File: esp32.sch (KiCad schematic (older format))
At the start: 5 parts, among them IC1 ESP32-WROVER-E_M213EH6464PH3Q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, J4 Bus_Connector

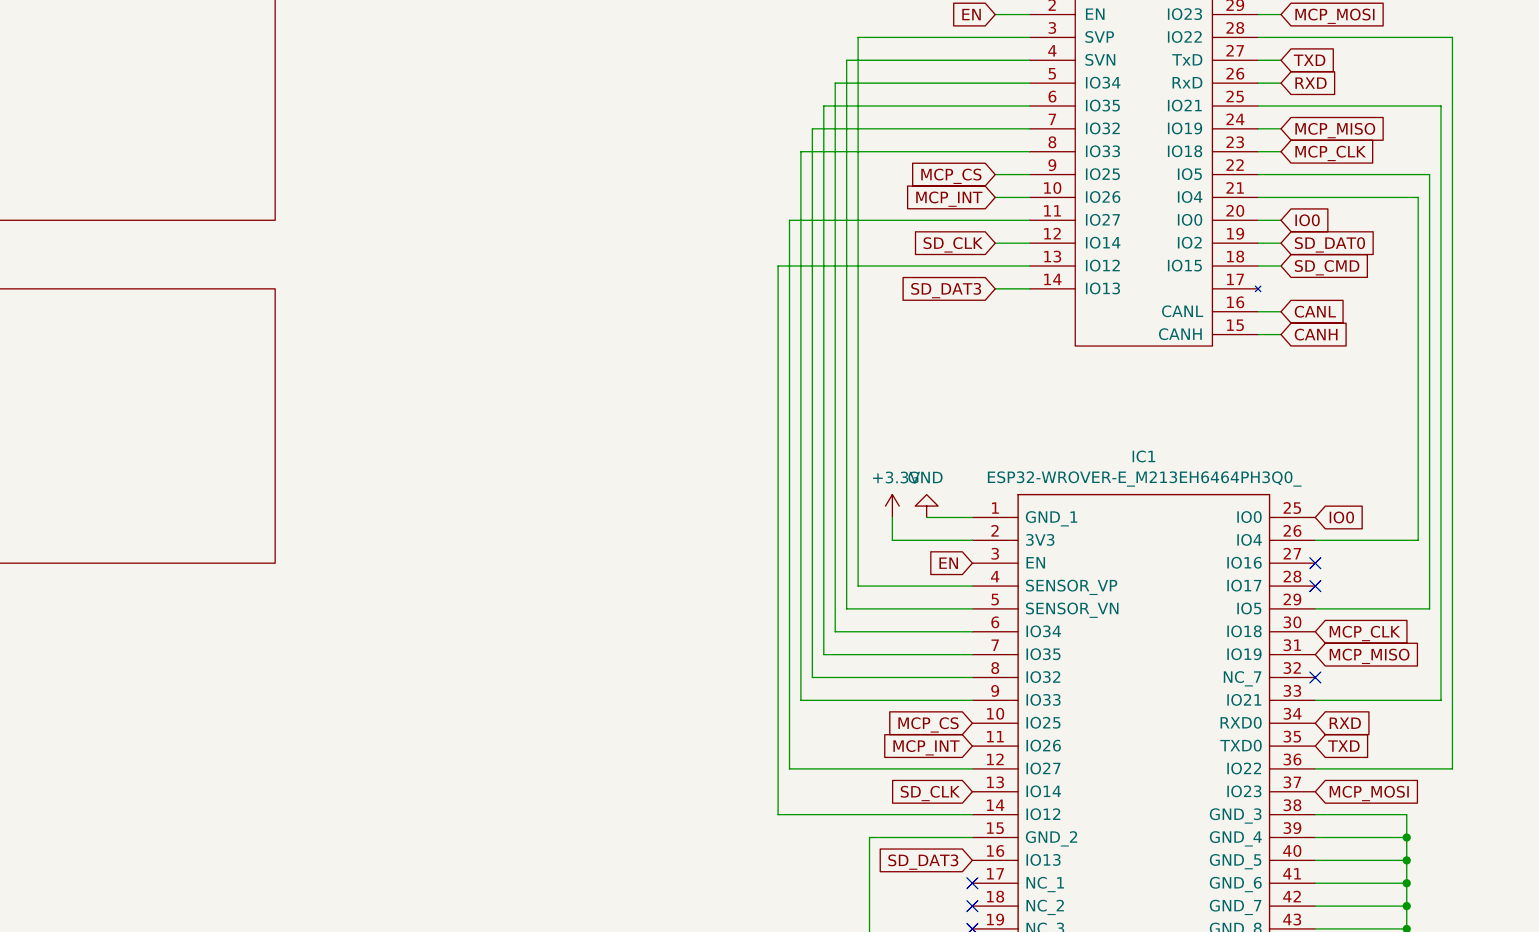
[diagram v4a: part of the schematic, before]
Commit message: Footprints für "Hand solder" Wahlweise MCP2518 oder interner CAN
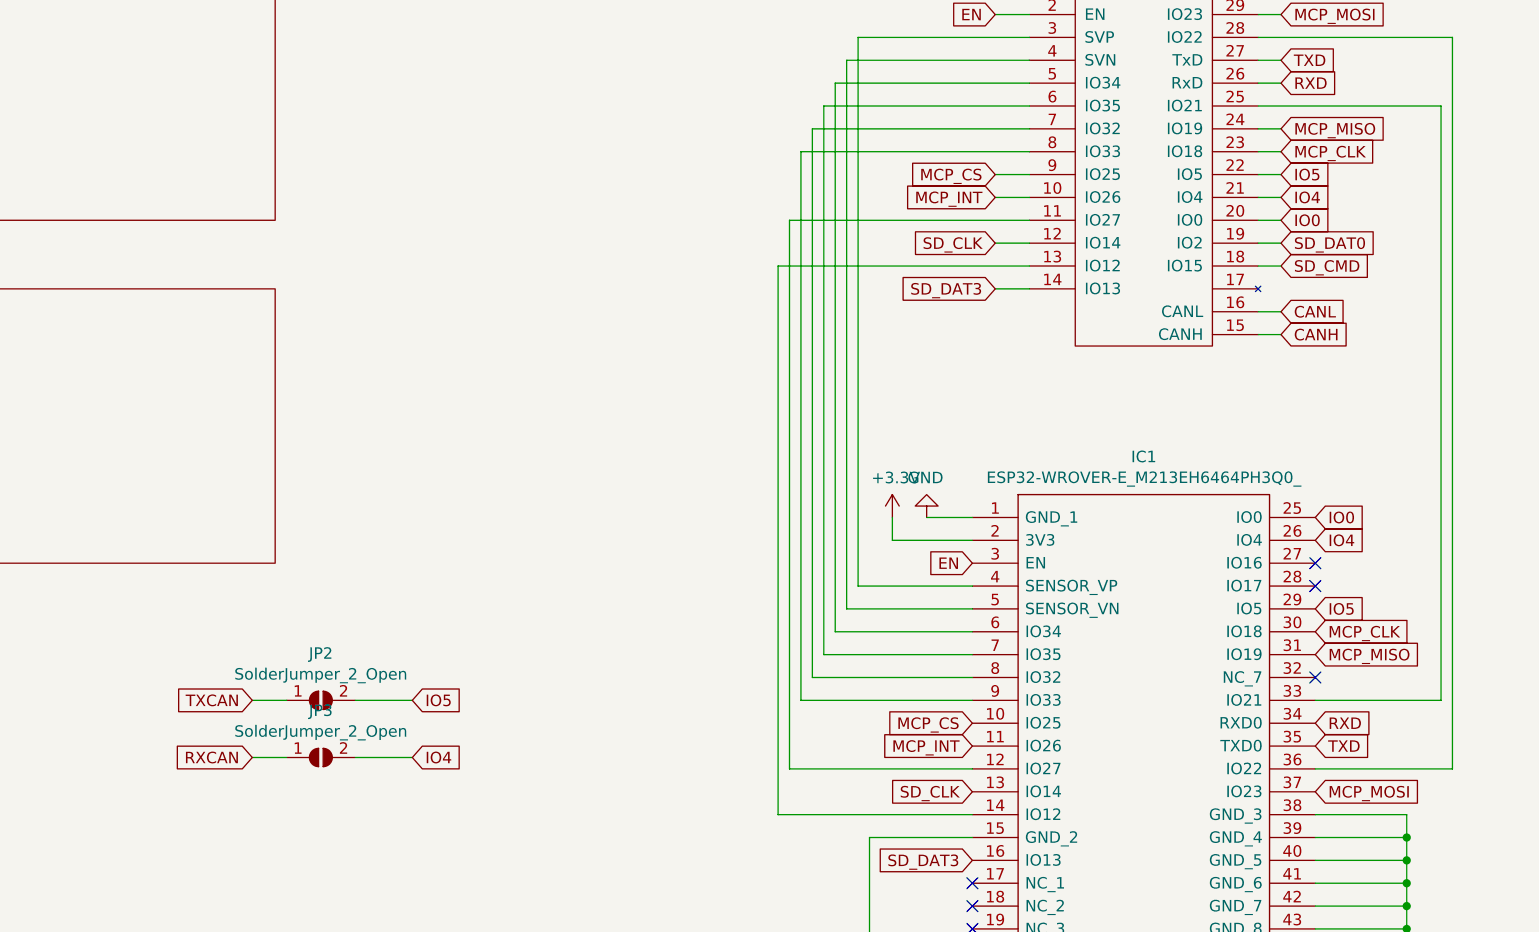
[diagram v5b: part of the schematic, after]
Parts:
- added JP2, JP3: SolderJumper_2_Open, Jumper:SolderJumper-2_P1.3mm_Open_RoundedPad1.0x1.5mm, symbol Jumper:SolderJumper_2_Open
- C1: footprint Capacitor_Tantalum_SMD:CP_EIA-3528-21_Kemet-B -> Capacitor_Tantalum_SMD:CP_EIA-3528-21_Kemet-B_Pad1.50x2.35mm_HandSolder
- C6: footprint Capacitor_SMD:C_0603_1608Metric -> Capacitor_SMD:C_0603_1608Metric_Pad1.08x0.95mm_HandSolder
- R7: footprint Resistor_SMD:R_0603_1608Metric -> Resistor_SMD:R_0603_1608Metric_Pad0.98x0.95mm_HandSolder
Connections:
- net IO4: now reaches IC1.26 (IO4), J4.21 (IO4)
- net IO4: now also JP3.2 (B)
- net IO5: now reaches IC1.29 (IO5), J4.22 (IO5)
- net IO5: now also JP2.2 (B)
- new net RXCAN: JP3.1 (A)
- new net TXCAN: JP2.1 (A)
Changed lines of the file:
@@
 F 0 "C1" H 2268 5896 50  0000 L CNN
 F 1 "10uF" H 2268 5805 50  0000 L CNN
-F 2 "Capacitor_Tantalum_SMD:CP_EIA-3528-21_Kemet-B" H 2188 5700 50  0001 C CNN
+F 2 "Capacitor_Tantalum_SMD:CP_EIA-3528-21_Kemet-B_Pad1.50x2.35mm_HandSolder" H 2188 5700 50  0001 C CNN
 F 3 "~" H 2150 5850 50  0001 C CNN
 	1    2150 5850
@@
 F 0 "R7" H 1420 4346 50  0000 L CNN
 F 1 "10k" H 1420 4255 50  0000 L CNN
-F 2 "Resistor_SMD:R_0603_1608Metric" V 1280 4300 50  0001 C CNN
+F 2 "Resistor_SMD:R_0603_1608Metric_Pad0.98x0.95mm_HandSolder" V 1280 4300 50  0001 C CNN
 F 3 "~" H 1350 4300 50  0001 C CNN
 	1    1350 4300
@@
 F 0 "C6" H 1465 4646 50  0000 L CNN
 F 1 "100nF" H 1465 4555 50  0000 L CNN
-F 2 "Capacitor_SMD:C_0603_1608Metric" H 1388 4450 50  0001 C CNN
+F 2 "Capacitor_SMD:C_0603_1608Metric_Pad1.08x0.95mm_HandSolder" H 1388 4450 50  0001 C CNN
 F 3 "~" H 1350 4600 50  0001 C CNN
 	1    1350 4600
@@
 	5400 2250 6500 2250
 Wire Wire Line
-	7750 3450 8200 3450
-Wire Wire Line
-	8200 3450 8200 1950
-Wire Wire Line
-	8200 1950 7500 1950
-Wire Wire Line
-	7750 3750 8250 3750
-Wire Wire Line
-	8250 3750 8250 1850
-Wire Wire Line
-	8250 1850 7500 1850
-Wire Wire Line
 	7750 4150 8300 4150
 Wire Wire Line
@@
 Wire Wire Line
 	7500 1050 7600 1050
+Text GLabel 3100 4150 0    50   Input ~ 0
+TXCAN
+Text GLabel 3100 4400 0    50   Input ~ 0
+RXCAN
+$Comp
+L Jumper:SolderJumper_2_Open JP2
+U 1 1 610C83D9
+P 3400 4150
+F 0 "JP2" H 3400 4355 50  0000 C CNN
+F 1 "SolderJumper_2_Open" H 3400 4264 50  0000 C CNN
+F 2 "Jumper:SolderJumper-2_P1.3mm_Open_RoundedPad1.0x1.5mm" H 3400 4150 50  0001 C CNN
+F 3 "~" H 3400 4150 50  0001 C CNN
+	1    3400 4150
+	1    0    0    -1
+$EndComp
+$Comp
+L Jumper:SolderJumper_2_Open JP3
+U 1 1 610C8E41
+P 3400 4400
+F 0 "JP3" H 3400 4605 50  0000 C CNN
+F 1 "SolderJumper_2_Open" H 3400 4514 50  0000 C CNN
+F 2 "Jumper:SolderJumper-2_P1.3mm_Open_RoundedPad1.0x1.5mm" H 3400 4400 50  0001 C CNN
+F 3 "~" H 3400 4400 50  0001 C CNN
+	1    3400 4400
+	1    0    0    -1
+$EndComp
+Text GLabel 7600 1950 2    50   Input ~ 0
+IO4
+Text GLabel 7600 1850 2    50   Input ~ 0
+IO5
+Text GLabel 7750 3450 2    50   Input ~ 0
+IO4
+Text GLabel 7750 3750 2    50   Input ~ 0
+IO5
+Text GLabel 3800 4400 2    50   Input ~ 0
+IO4
+Text GLabel 3800 4150 2    50   Input ~ 0
+IO5
+Wire Wire Line
+	7500 1850 7600 1850
+Wire Wire Line
+	7500 1950 7600 1950
+Wire Wire Line
+	3100 4150 3250 4150
+Wire Wire Line
+	3100 4400 3250 4400
+Wire Wire Line
+	3550 4150 3800 4150
+Wire Wire Line
+	3550 4400 3800 4400
 $EndSCHEMATC

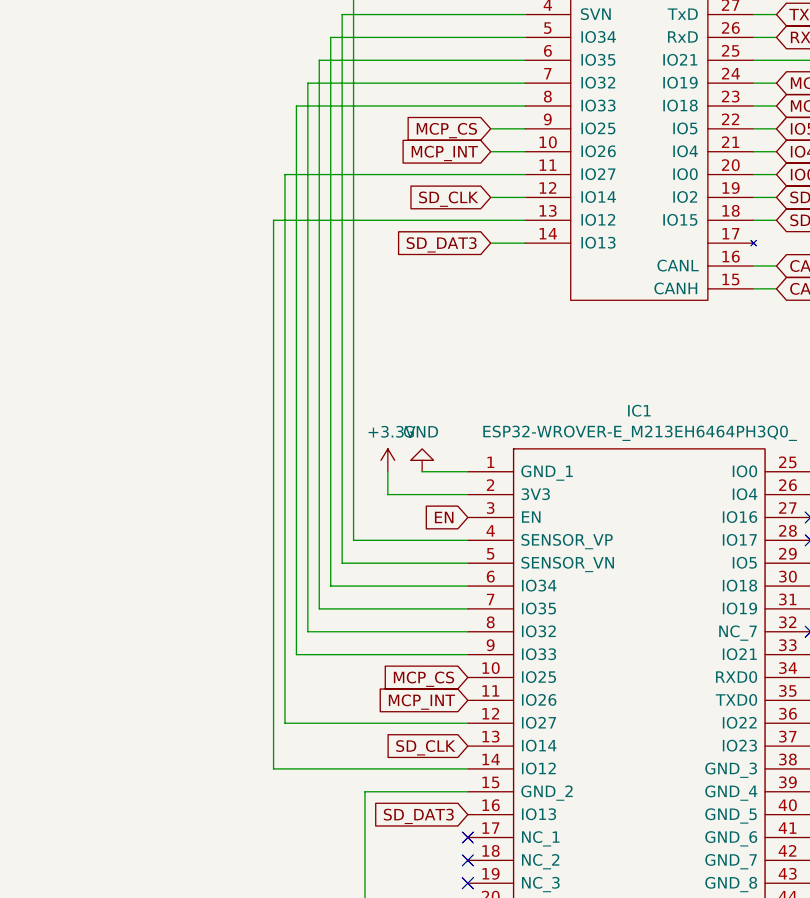
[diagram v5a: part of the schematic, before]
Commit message: - SN65 RS an GPIO 27 - Quarz Footprint 3225
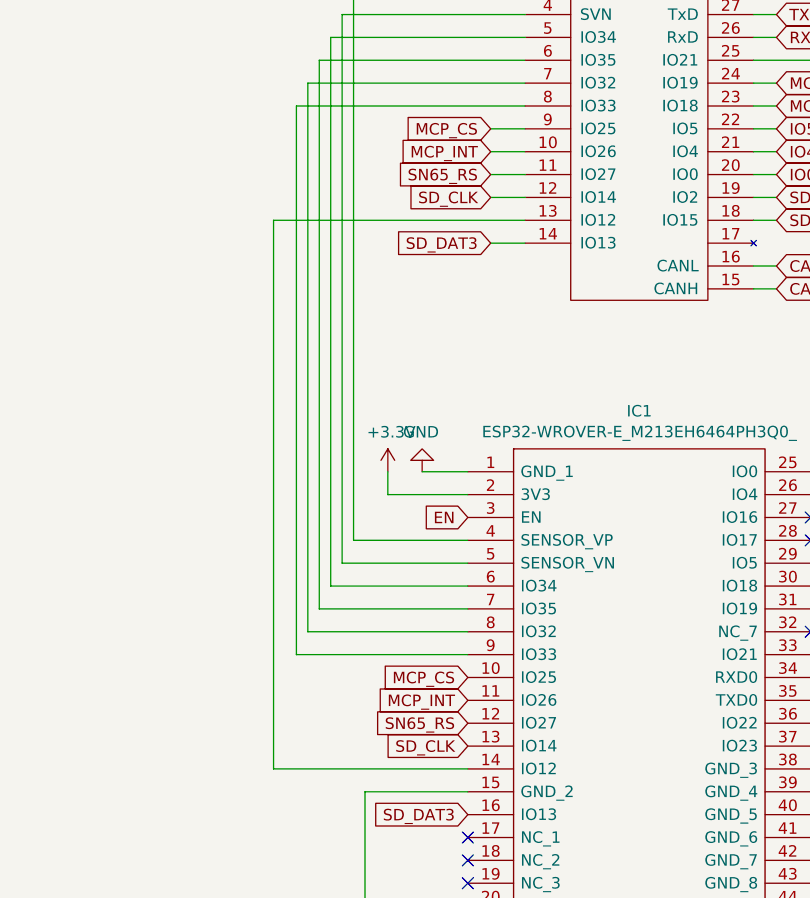
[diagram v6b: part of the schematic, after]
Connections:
- net SN65_RS: now reaches IC1.12 (IO27), J4.11 (IO27)
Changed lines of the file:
@@
 	5500 1750 6500 1750
-Wire Wire Line
-	6250 4450 5450 4450
-Wire Wire Line
-	5450 4450 5450 2050
-Wire Wire Line
-	5450 2050 6500 2050
 Wire Wire Line
 	6250 4650 5400 4650
@@
 Wire Wire Line
 	3550 4400 3800 4400
+Text GLabel 6250 4450 0    50   Input ~ 0
+SN65_RS
+Text GLabel 6350 2050 0    50   Input ~ 0
+SN65_RS
+Wire Wire Line
+	6350 2050 6500 2050
 $EndSCHEMATC
